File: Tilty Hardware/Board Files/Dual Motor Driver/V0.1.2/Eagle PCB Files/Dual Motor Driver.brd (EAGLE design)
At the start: 38.4 x 50.8 mm, 42 parts, among them J1 AVR_SPI_PRG_62X3_LOCK, Q1 16MHz, U1 ATMEGA328P, U2 L298_BRIDGE_DRIVER, U3 LM2931

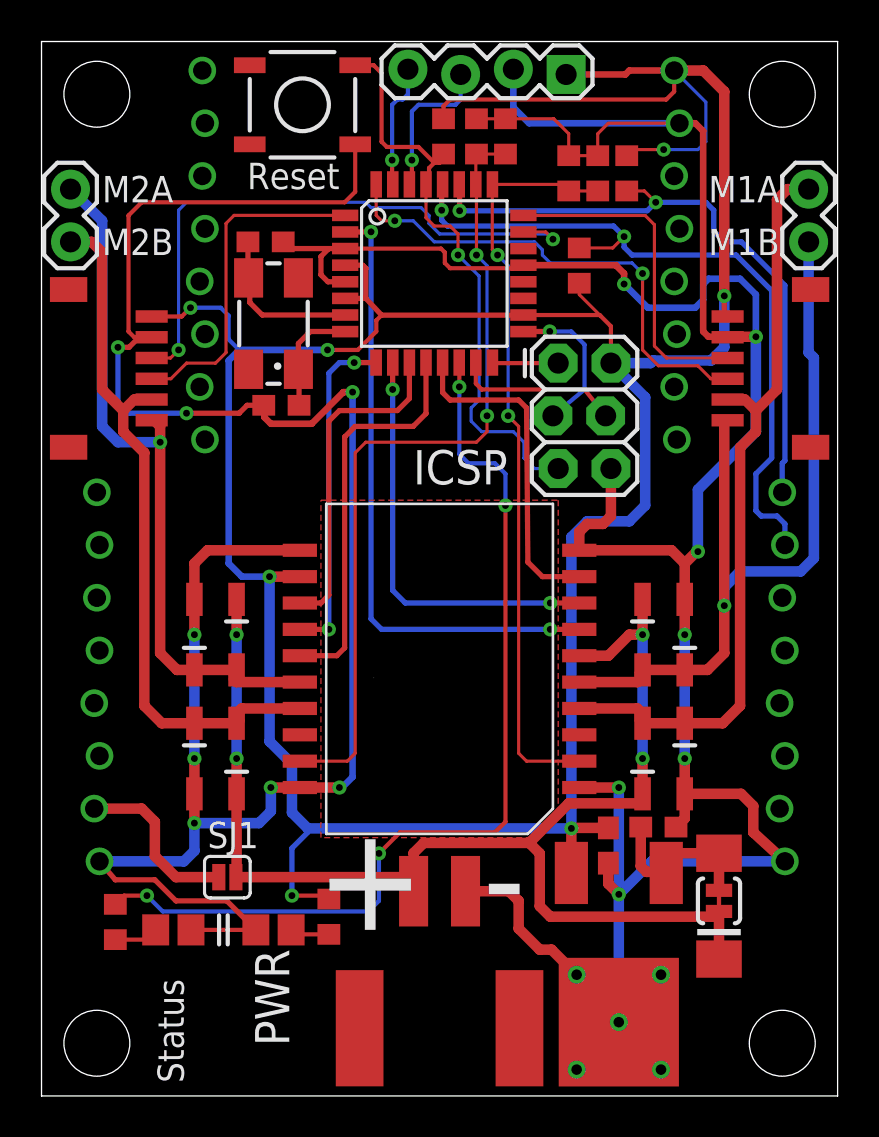
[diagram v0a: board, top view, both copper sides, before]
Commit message: Dula motor driver revisions
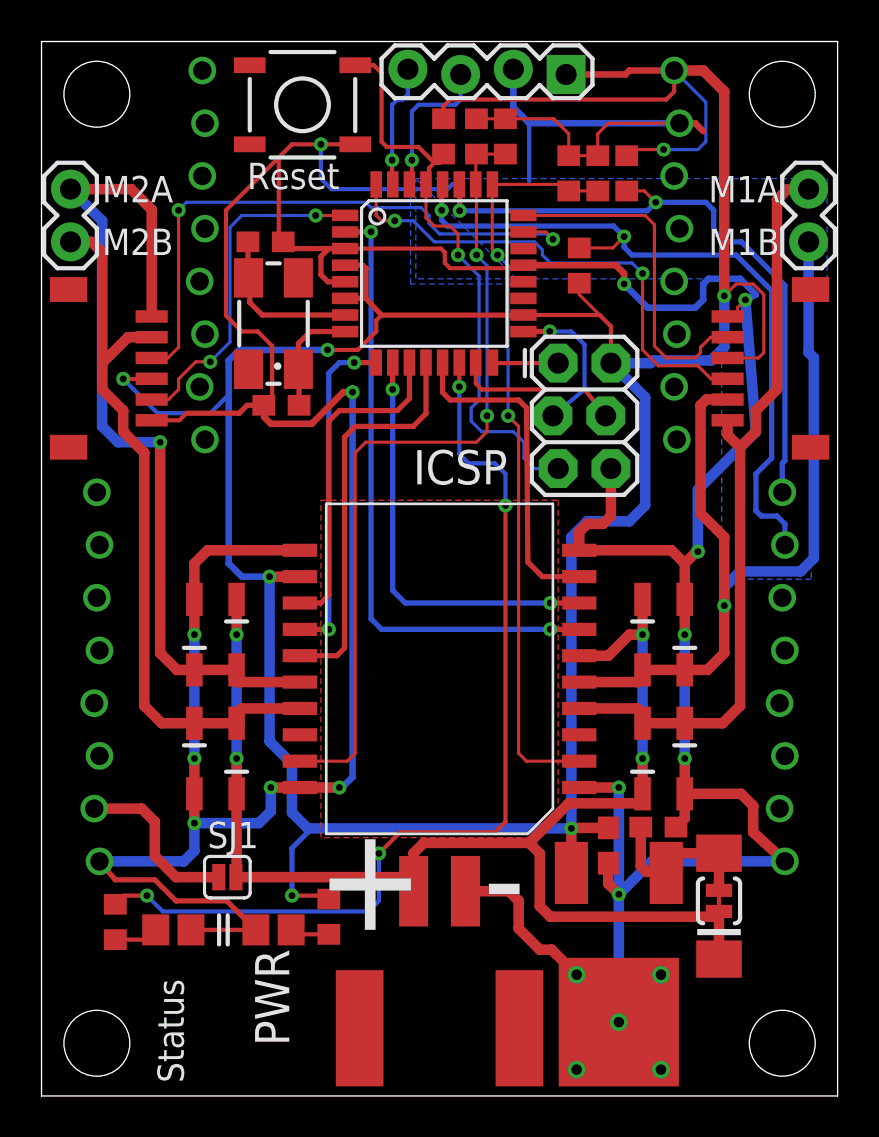
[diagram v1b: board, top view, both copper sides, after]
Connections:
- net +5V: now also JP5.P$4, JP6.P$4; no longer JP5.P$1, JP6.P$6
- net ENC1B: now also JP6.P$5; no longer JP6.P$4
- net ENC2B: now also JP5.P$5; no longer JP5.P$4
- net GND: now also JP5.P$6, JP6.P$6; no longer JP5.P$2, JP6.P$5
- net M1A: now also JP6.P$1; no longer JP6.P$2
- net M1B: now also JP6.P$2; no longer JP6.P$1
- net M2A: now also JP5.P$1; no longer JP5.P$6
- net M2B: now also JP5.P$2; no longer JP5.P$5
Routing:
- net +5V: track 157.9 -> 167.1 mm
- net M2A: track 34.4 -> 42.6 mm
- net GND: track 259.0 -> 256.3 mm, vias 20 -> 19
- net M1B: track 40.2 -> 42.7 mm
- net M2B: track 34.4 -> 35.7 mm
- net ENC1B: track 16.1 -> 16.7 mm
- net ENC2B: track 16.2 -> 16.5 mm, vias 0 -> 2
- added copper zone on layer 16, net GND

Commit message: Motor driver updates
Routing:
- net M1B: track 42.7 -> 44.6 mm
- net +5V: track 167.1 -> 166.2 mm
- net GND: vias 19 -> 26
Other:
- board text added: "v0.1.2"
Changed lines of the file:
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@@
 <rectangle x1="24.92741875" y1="19.961690625" x2="25.394775" y2="19.982009375" layer="26" rot="R213"/>
 <rectangle x1="22.662809375" y1="18.688978125" x2="23.739765625" y2="18.709296875" layer="26" rot="R213"/>
-<rectangle x1="16.003228125" y1="20.133675" x2="16.023546875" y2="20.15399375" layer="25" rot="R327"/>
+<rectangle x1="16.003228125" y1="20.133675" x2="16.023546875" y2="20.15399375" layer="26" rot="R327"/>
 <rectangle x1="24.914709375" y1="19.984265625" x2="25.402390625" y2="20.004584375" layer="26" rot="R213"/>
 <rectangle x1="22.6484625" y1="18.7170875" x2="23.7660625" y2="18.73740625" layer="26" rot="R213"/>
@@
 <wire x1="28.448" y1="15.621" x2="29.464" y2="15.621" width="0.2032" layer="25"/>
 <wire x1="30.48" y1="16.891" x2="31.496" y2="16.891" width="0.2032" layer="25"/>
+<text x="24.384" y="11.176" size="1.524" layer="26" ratio="12" rot="MR0">v0.1.2</text>
 </plain>
 <attributes>
@@
 <vertex x="37.846" y="39.116"/>
 <vertex x="37.084" y="39.116"/>
-<vertex x="37.084" y="24.892"/>
-<vertex x="32.766" y="24.892"/>
+<vertex x="37.084" y="25.146"/>
+<vertex x="32.766" y="25.146"/>
 <vertex x="32.766" y="39.37"/>
 <vertex x="18.034" y="39.37"/>
@@
 <wire x1="5.30635" y1="32.552" x2="6.644" y2="32.552" width="0.2032" layer="1"/>
 <wire x1="6.644" y1="32.552" x2="6.985" y2="32.893" width="0.2032" layer="1"/>
-<polygon width="0.2032" layer="16" pour="cutout">
+<polygon width="0.2032" layer="16">
 <vertex x="17.78" y="39.116"/>
 <vertex x="17.78" y="43.18"/>
@@
 <wire x1="8.89" y1="37.592" x2="8.89" y2="42.672" width="0.2032" layer="1"/>
 <wire x1="8.89" y1="42.672" x2="11.43" y2="45.212" width="0.2032" layer="1"/>
+<polygon width="0.1524" layer="16">
+<vertex x="0.508" y="0.508"/>
+<vertex x="37.846" y="0.508"/>
+<vertex x="37.846" y="50.292"/>
+<vertex x="0.508" y="50.292"/>
+</polygon>
+<via x="21.082" y="27.432" extent="1-16" drill="0.381"/>
+<via x="18.288" y="27.432" extent="1-16" drill="0.381"/>
+<via x="18.288" y="24.892" extent="1-16" drill="0.381"/>
+<via x="21.082" y="24.892" extent="1-16" drill="0.381"/>
+<via x="21.082" y="18.034" extent="1-16" drill="0.381"/>
+<via x="20.066" y="14.986" extent="1-16" drill="0.381"/>
+<polygon width="0.1524" layer="1">
+<vertex x="15.494" y="43.18"/>
+<vertex x="22.606" y="43.18"/>
+<vertex x="22.606" y="36.068"/>
+<vertex x="15.494" y="36.068"/>
+</polygon>
+<via x="18.034" y="36.83" extent="1-16" drill="0.3302"/>
 </signal>
 <signal name="M1A">
@@
 <wire x1="32.082" y1="20.525" x2="32.893" y2="21.336" width="0.508" layer="1"/>
 <contactref element="JP9" pad="1"/>
-<via x="32.893" y="23.622" extent="1-16" drill="0.3302"/>
-<wire x1="32.893" y1="21.336" x2="32.893" y2="23.622" width="0.508" layer="1"/>
-<wire x1="32.893" y1="23.622" x2="32.893" y2="24.511" width="0.508" layer="16"/>
-<wire x1="32.893" y1="24.511" x2="33.655" y2="25.273" width="0.508" layer="16"/>
-<wire x1="33.655" y1="25.273" x2="36.576" y2="25.273" width="0.508" layer="16"/>
-<wire x1="36.576" y1="25.273" x2="37.211" y2="25.908" width="0.508" layer="16"/>
-<wire x1="37.211" y1="25.908" x2="37.211" y2="35.56" width="0.508" layer="16"/>
-<wire x1="37.211" y1="35.56" x2="36.957" y2="35.814" width="0.508" layer="16"/>
-<wire x1="36.957" y1="35.814" x2="36.957" y2="41.148" width="0.508" layer="16"/>
+<via x="32.893" y="21.336" extent="1-16" drill="0.3302"/>
+<wire x1="37.211" y1="23.495" x2="37.211" y2="39.624" width="0.508" layer="16"/>
+<wire x1="37.211" y1="39.624" x2="36.957" y2="39.878" width="0.508" layer="16"/>
+<wire x1="36.957" y1="39.878" x2="36.957" y2="41.148" width="0.508" layer="16"/>
 <contactref element="JP6" pad="P$2"/>
 <wire x1="33.054" y1="33.552" x2="32.028" y2="33.552" width="0.508" layer="1"/>
@@
 <wire x1="31.75" y1="33.274" x2="31.75" y2="28.067" width="0.508" layer="1"/>
 <wire x1="31.75" y1="28.067" x2="32.893" y2="26.924" width="0.508" layer="1"/>
-<wire x1="32.893" y1="26.924" x2="32.893" y2="23.622" width="0.508" layer="1"/>
+<wire x1="32.893" y1="26.924" x2="32.893" y2="21.336" width="0.508" layer="1"/>
+<wire x1="32.893" y1="21.336" x2="34.29" y2="22.733" width="0.508" layer="16"/>
+<wire x1="34.29" y1="22.733" x2="36.449" y2="22.733" width="0.508" layer="16"/>
+<wire x1="36.449" y1="22.733" x2="37.211" y2="23.495" width="0.508" layer="16"/>
 </signal>
 <signal name="M2A">
@@
 <wire x1="9.525" y1="18.542" x2="9.525" y2="18.083" width="0.508" layer="1"/>
 <wire x1="9.525" y1="18.083" x2="9.398" y2="17.956" width="0.508" layer="1"/>
-<wire x1="3.937" y1="33.02" x2="3.937" y2="32.004" width="0.508" layer="1"/>
-<wire x1="3.937" y1="32.004" x2="4.953" y2="30.988" width="0.508" layer="1"/>
 <wire x1="4.953" y1="30.988" x2="4.953" y2="18.796" width="0.508" layer="1"/>
 <wire x1="7.366" y1="17.956" x2="5.793" y2="17.956" width="0.508" layer="1"/>
@@
 <wire x1="2.413" y1="41.148" x2="2.921" y2="40.64" width="0.508" layer="1"/>
 <wire x1="2.921" y1="40.64" x2="2.921" y2="35.306" width="0.508" layer="1"/>
-<wire x1="2.921" y1="35.306" x2="2.921" y2="34.036" width="0.508" layer="1"/>
-<wire x1="2.921" y1="34.036" x2="3.937" y2="33.02" width="0.508" layer="1"/>
+<wire x1="2.921" y1="35.306" x2="2.921" y2="33.02" width="0.508" layer="1"/>
 <contactref element="JP5" pad="P$2"/>
 <wire x1="5.30635" y1="36.552" x2="4.167" y2="36.552" width="0.508" layer="1"/>
 <wire x1="4.167" y1="36.552" x2="2.921" y2="35.306" width="0.508" layer="1"/>
+<wire x1="4.953" y1="30.988" x2="2.921" y2="33.02" width="0.508" layer="1"/>
 </signal>
 <signal name="+24V">
@@
 <contactref element="JP6" pad="P$4"/>
 <contactref element="JP5" pad="P$4"/>
-<wire x1="33.054" y1="35.552" x2="34.536" y2="35.552" width="0.1524" layer="1"/>
-<wire x1="34.536" y1="35.552" x2="34.798" y2="35.814" width="0.1524" layer="1"/>
-<wire x1="34.798" y1="35.814" x2="34.798" y2="38.608" width="0.1524" layer="1"/>
-<wire x1="34.798" y1="38.608" x2="34.29" y2="39.116" width="0.1524" layer="1"/>
-<wire x1="34.29" y1="39.116" x2="33.4645" y2="39.116" width="0.1524" layer="1"/>
-<wire x1="33.4645" y1="39.116" x2="32.893" y2="38.5445" width="0.1524" layer="1"/>
+<wire x1="33.3375" y1="38.989" x2="32.893" y2="38.5445" width="0.1524" layer="1"/>
 <via x="3.937" y="34.544" extent="1-16" drill="0.3302"/>
 <wire x1="3.937" y1="34.544" x2="5.29835" y2="34.544" width="0.2032" layer="1"/>
@@
 <wire x1="8.128" y1="32.893" x2="5.588" y2="32.893" width="0.2032" layer="16"/>
 <wire x1="5.588" y1="32.893" x2="3.937" y2="34.544" width="0.2032" layer="16"/>
+<wire x1="33.3375" y1="38.989" x2="34.163" y2="38.989" width="0.1524" layer="1"/>
+<wire x1="34.163" y1="38.989" x2="34.544" y2="38.608" width="0.1524" layer="1"/>
+<wire x1="34.544" y1="38.608" x2="34.544" y2="38.1" width="0.1524" layer="1"/>
+<wire x1="34.544" y1="38.1" x2="34.0995" y2="37.6555" width="0.1524" layer="1"/>
+<wire x1="34.0995" y1="37.6555" x2="34.0995" y2="35.8775" width="0.1524" layer="1"/>
+<wire x1="34.0995" y1="35.8775" x2="33.782" y2="35.56" width="0.1524" layer="1"/>
+<wire x1="33.782" y1="35.56" x2="33.062" y2="35.56" width="0.1524" layer="1"/>
+<wire x1="33.062" y1="35.56" x2="33.054" y2="35.552" width="0.1524" layer="1"/>
 </signal>
 <signal name="RESET">
